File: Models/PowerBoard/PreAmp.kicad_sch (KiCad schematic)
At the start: 2 parts, among them U2 LM7805, 5V, 5%, U4 LM7905, -5V, 5%

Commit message: Save progress
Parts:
- added C10, C9: 1 uF, 0603, symbol Device:C
- added C5: 220 nF, 0603, symbol Device:C
- added C6: 100 nF, 0603, symbol Device:C
- added D3, D5: D_Schottky, symbol Device:D_Schottky
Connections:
- net at U2.1 (IN): now also C5.1
- net GND: now reaches U2.2 (GND)
- net GND: now also U4.1 (GND), C10.2, C5.2, C6.2, C9.1, D3.2 (A), D5.1 (K)
- net at U2.3 (OUT): now also C6.1, D3.1 (K)
- net at U4.2 (IN): now also C10.1
- net at U4.3 (OUT): now also C9.2, D5.2 (A)

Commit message: Save progres
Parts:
- added D12: 1N4007W, symbol Device:D
- added D7: D_Zener, symbol Custom:D_Zener
- added RV1: R_Potentiometer_US, symbol Device:R_Potentiometer_US
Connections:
- net -5V: now reaches C9.2, D5.2 (A), U4.3 (OUT)
- net 18V: now reaches C5.1, U2.1 (IN)
- net 5V: now reaches C6.1, D3.1 (K), U2.3 (OUT)
- net -18V: now reaches C10.1, U4.2 (IN)

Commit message: Save progress
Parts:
- removed D5: D_Schottky, symbol Device:D_Schottky
- removed D7: D_Zener, symbol Custom:D_Zener
- added C13, C14: 10 uF, 0805, symbol Device:C
- added D13: D_Schottky, symbol Device:D_Schottky
- added D5: 1N4007W, symbol Device:D
- added NT11, NT12, NT3, NT4: NetTie_2, symbol Device:NetTie_2
- added RV2: 1k, 10%, symbol Device:R_Potentiometer_US
- RV1: value R_Potentiometer_US -> 1k, 10%
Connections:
- net -18V: now also NT12.2; no longer C10.1, U4.2 (IN)
- net -5V: now also NT11.2, RV2.1; no longer C9.2, U4.3 (OUT)
- net 18V: now also NT4.1; no longer C5.1, U2.1 (IN)
- net 5V: now also RV1.3, NT3.2; no longer C6.1, D3.1 (K), U2.3 (OUT)
- net GND: now also RV1.1, C13.2, C14.1, D13.1 (K), RV2.3
- net at D12.1 (K): now also C5.1, U2.1 (IN), NT4.2
- net at D12.2 (A): now also C6.1, D3.1 (K), U2.3 (OUT), NT3.1
- net 2.5V: now reaches RV1.2
- net 2.5V: now also C13.1
- new net: C9.2, D13.2 (A), D5.1 (K), NT11.1, U4.3 (OUT)
- new net: C10.1, D5.2 (A), NT12.1, U4.2 (IN)
- new net -1.5V: C14.2, RV2.2
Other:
- moved on the sheet: RV1

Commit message: Save progress
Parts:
- removed NT11, NT12, NT3, NT4: NetTie_2, symbol Device:NetTie_2
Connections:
- net -18V: now also C10.1, D5.2 (A), U4.2 (IN)
- net -5V: now also C9.2, D13.2 (A), D5.1 (K), U4.3 (OUT)
- net 18V: now also C5.1, D12.1 (K), U2.1 (IN)
- net 5V: now also C6.1, D12.2 (A), D3.1 (K), U2.3 (OUT)

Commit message: Save progress
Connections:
- net -5V renamed -5V_PreAmp
- net 5V renamed 5V_PreAmp
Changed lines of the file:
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@@
 		)
 	)
-	(label "-5V"
-		(at 132.08 132.08 0)
+	(global_label "5V_PreAmp"
+		(shape output)
+		(at 139.7 55.88 0)
+		(fields_autoplaced yes)
 		(effects
 			(font
 				(size 1.27 1.27)
 			)
-			(justify left bottom)
+			(justify left)
+		)
+		(property "Intersheetrefs" "${INTERSHEET_REFS}"
+			(at 153.0266 55.88 0)
+			(effects
+				(font
+					(size 1.27 1.27)
+				)
+				(justify left)
+				(hide yes)
+			)
 		)
 	)
-	(label "5V"
-		(at 139.7 55.88 0)
+	(global_label "-5V_PreAmp"
+		(shape output)
+		(at 203.2 124.46 270)
+		(fields_autoplaced yes)
 		(effects
 			(font
 				(size 1.27 1.27)
 			)
-			(justify left bottom)
+			(justify right)
+		)
+		(property "Intersheetrefs" "${INTERSHEET_REFS}"
+			(at 203.2 139.359 90)
+			(effects
+				(font
+					(size 1.27 1.27)
+				)
+				(justify right)
+				(hide yes)
+			)
 		)
 	)
-	(label "5V"
-		(at 203.2 43.18 0)
+	(global_label "-5V_PreAmp"
+		(shape output)
+		(at 132.08 132.08 0)
+		(fields_autoplaced yes)
 		(effects
 			(font
 				(size 1.27 1.27)
 			)
-			(justify left bottom)
+			(justify left)
+		)
+		(property "Intersheetrefs" "${INTERSHEET_REFS}"
+			(at 146.979 132.08 0)
+			(effects
+				(font
+					(size 1.27 1.27)
+				)
+				(justify left)
+				(hide yes)
+			)
 		)
 	)
-	(label "-5V"
-		(at 203.2 124.46 0)
+	(global_label "5V_PreAmp"
+		(shape output)
+		(at 203.2 43.18 90)
+		(fields_autoplaced yes)
 		(effects
 			(font
 				(size 1.27 1.27)
 			)
-			(justify left bottom)
+			(justify left)
+		)
+		(property "Intersheetrefs" "${INTERSHEET_REFS}"
+			(at 203.2 29.8534 90)
+			(effects
+				(font
+					(size 1.27 1.27)
+				)
+				(justify left)
+				(hide yes)
+			)
 		)
 	)

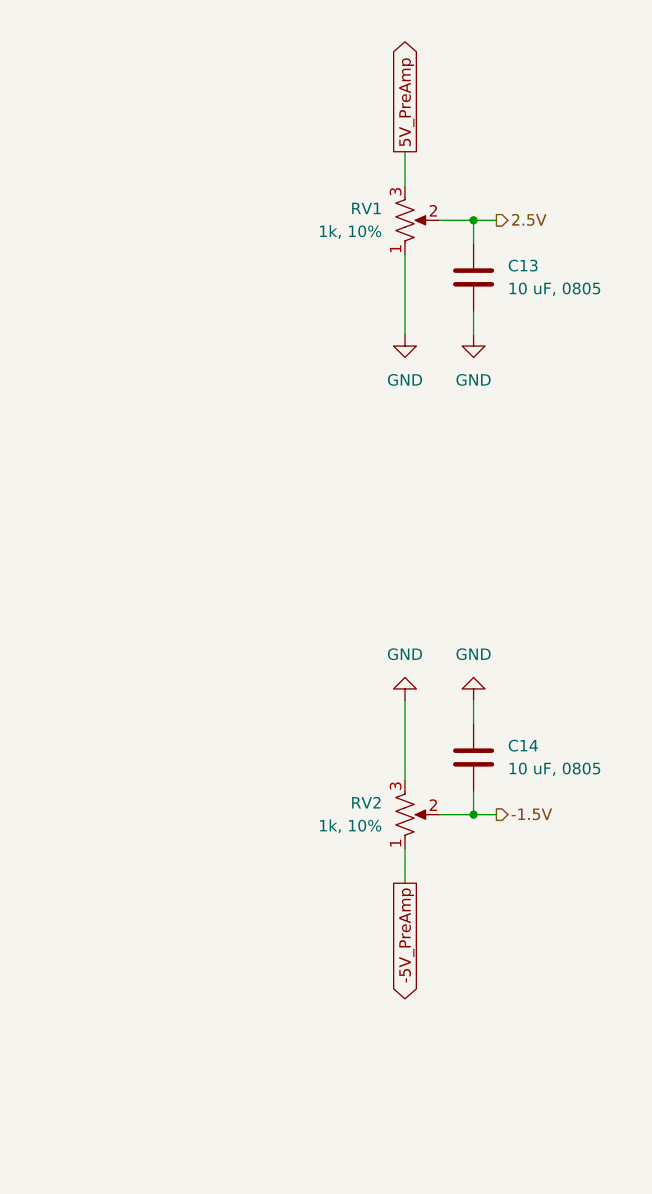
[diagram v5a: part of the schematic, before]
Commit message: Connectors should be fully specified now
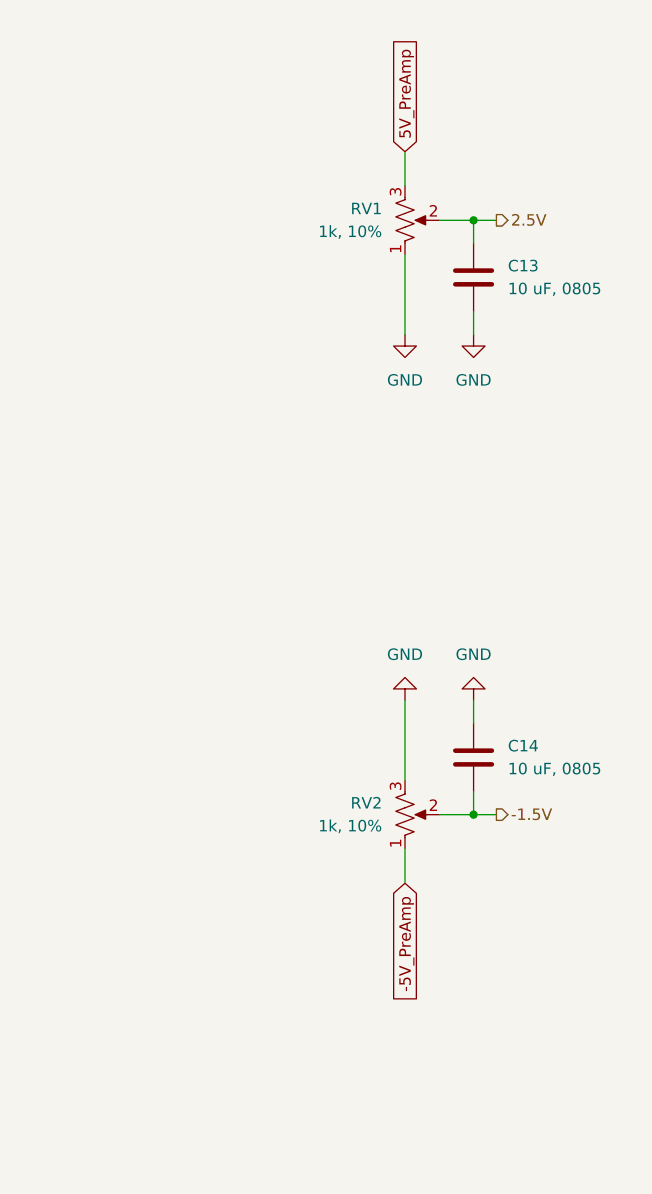
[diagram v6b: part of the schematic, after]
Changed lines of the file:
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@@
 	)
 	(global_label "-5V_PreAmp"
-		(shape output)
+		(shape input)
 		(at 203.2 124.46 270)
 		(fields_autoplaced yes)
@@
 	)
 	(global_label "5V_PreAmp"
-		(shape output)
+		(shape input)
 		(at 203.2 43.18 90)
 		(fields_autoplaced yes)

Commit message: Passes ERC
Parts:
- removed U2: LM7805, 5V, 5%, symbol Vendor:LM78
- removed U4: LM7905, -5V, 5%, symbol Vendor:LM79
- added U5: LM7805, 5V, 5%, symbol Vendor:LM78
- added U6: LM7905, -5V, 5%, symbol Vendor:LM79
- renumbered C9 to C10, C10 to C11, C6 to C12, C5 to C9, D5 to D10, D13 to D11, D3 to D12, D12 to D9
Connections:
- net -18V: now also U6.2 (IN)
- net -5V_PreAmp: now also U6.3 (OUT)
- net 18V: now also U5.1 (IN)
- net 5V_PreAmp: now also U5.3 (OUT)
- net GND: now also U5.2 (GND), U6.1 (GND)

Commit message: Save progress
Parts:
- D10, D9: Cost (none) -> $0.059
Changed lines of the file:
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@@
+			)
+		)
+		(property "Cost" "$0.059"
+			(at 86.36 38.1 0)
+			(effects
+				(font
+					(size 1.27 1.27)
+				)
+				(hide yes)
 			)
 		)
@@
 			(effects
 				(font
+					(size 1.27 1.27)
+				)
+				(hide yes)
+			)
+		)
+		(property "Cost" "$0.059"
+			(at 111.76 135.89 90)
+			(effects
+				(font
